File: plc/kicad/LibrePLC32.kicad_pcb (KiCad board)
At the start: 4 copper layers, 285 parts, among them CN1 DB128V-5.08-2P-GN-S, CN10 DB128V-5.08-6P-GN-S, CN11 DB2ERC-5.08-4P, CN12 DB2ERC-5.08-4P, CN2 DB128V-5.08-2P-GN-S, CN3 DB128V-5.08-2P-GN-S, CN4 DB128V-5.08-2P-GN-S, CN5 DB128V-5.08-2P-GN-S, CN6 DB128V-5.08-2P-GN-S, CN7 DB128V-5.08-2P-GN-S, CN8 DB128V-5.08-2P-GN-S, CN9 DB128V-5.08-2P-GN-S, J2 Conn_01x04_Pin, J3 Conn_01x02_Pin, Q1 AO3400A, Q2 AO3400A, Q3 L8050QLT1G, Q4 L8050QLT1G, Q5 BSS138LT1G, Q6 CSD19537Q3, SW1 TSD003B08026A03, SW2 TSD003B08026A03, SW3 TSD003B08026A03, SW4 MSK12C02, SW5 MSK12C02, U1 TCA9535PWR, U10 ESP32-S3-MINI-1U, U11 BS-0601-SK-4W, U12 AHT20_C2757850, U13 CP2102N-A02-GQFN28R, U14 LMR16006XDDCR, U15 TPS7A5201QRGRRQ1, U16 TPS26630RGER, U18 TCAN337DR, U19 THVD1450DR, U2 TPS272C45DRHFR, U20 W5500, U21 TPS54560BDDAR, U3 TPS272C45DRHFR, U4 ADS1115IDGSR, U5 LTV-814S-TA1-A, U6 LTV-814S-TA1-A, U7 LTV-814S-TA1-A, U8 LTV-814S-TA1-A, U9 RV-3028-C7, X1 X322525MRB4SI

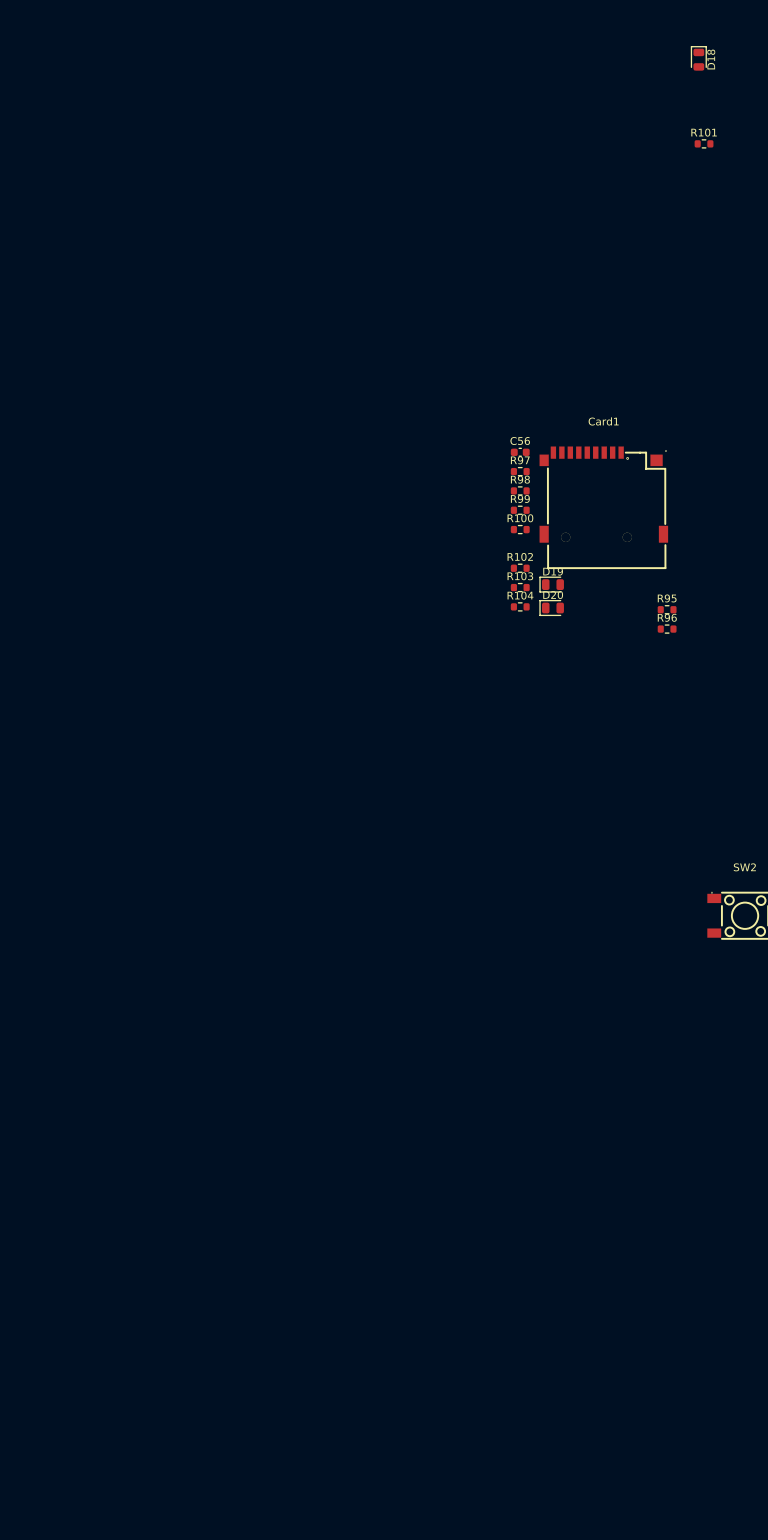
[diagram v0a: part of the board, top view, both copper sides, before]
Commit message: SD Card PCB Placement
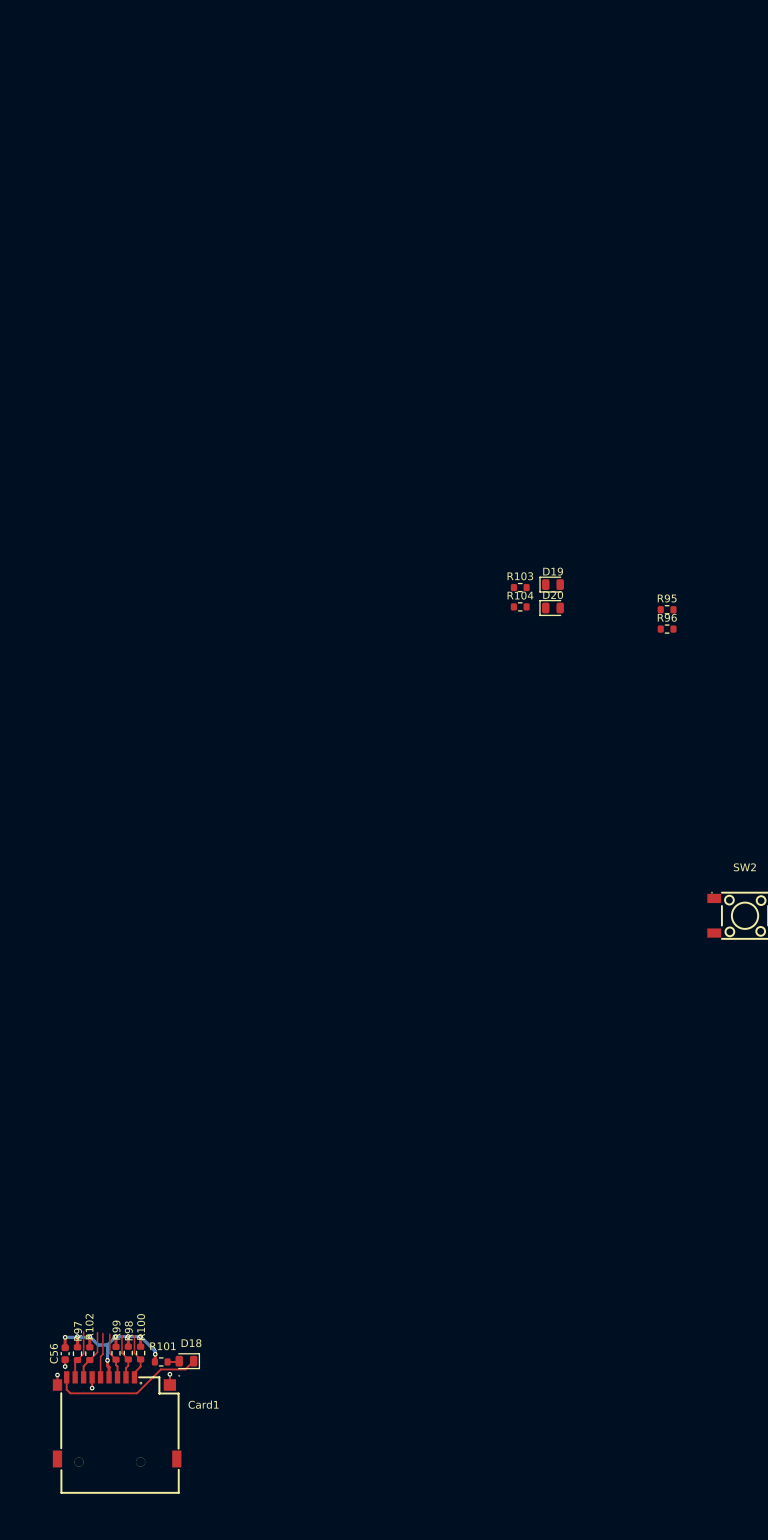
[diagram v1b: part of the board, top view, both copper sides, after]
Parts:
- moved D18 181.7 mm to (6.95, 280.1), turned to 180 degrees
- moved R101 173.2 mm to (3.67, 280.2), turned to 180 degrees
- moved Card1 135.7 mm to (-2.05, 287.5)
- moved C56 131.1 mm to (-8.80, 279.1), turned to 90 degrees
- moved R97 128.2 mm to (-7.20, 279.1), turned to 90 degrees
- moved R98 123.0 mm to (-0.60, 279.1), turned to 90 degrees
- moved R99 121.4 mm to (-2.20, 279.1), turned to 90 degrees
- moved R100 117.8 mm to (1.00, 279.1), turned to 90 degrees
- moved R102 116.3 mm to (-5.60, 279.1), turned to 90 degrees
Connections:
- Card1 pad CD: GND -> /MCU/SD_CD
- D18 pad 1: GND -> /MCU/SD_CD
- TP7 pad 1: GND -> /MCU/SD_CD
- U10 pad 11: GND -> /MCU/SD_CD
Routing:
- net +3V3: track 60.4 -> 87.5 mm, vias 5 -> 13
- net /MCU/SD_CD: track 0.00 -> 20.3 mm
- net /Ethernet/SPI_MISO: track 10.6 -> 17.1 mm
- net /MCU/SD_DAT1: track 0.00 -> 6.36 mm
- net /MCU/SD_DAT2: track 0.00 -> 6.06 mm
- net /Ethernet/SPI_MOSI: track 9.64 -> 15.7 mm
- net /MCU/~{SD_CS}: track 0.00 -> 5.88 mm
- net /Ethernet/SPI_SCLK: track 11.6 -> 17.4 mm
- net GND: track 97.2 -> 102.1 mm, vias 78 -> 82
- net Net-(D18-A): track 0.00 -> 1.55 mm

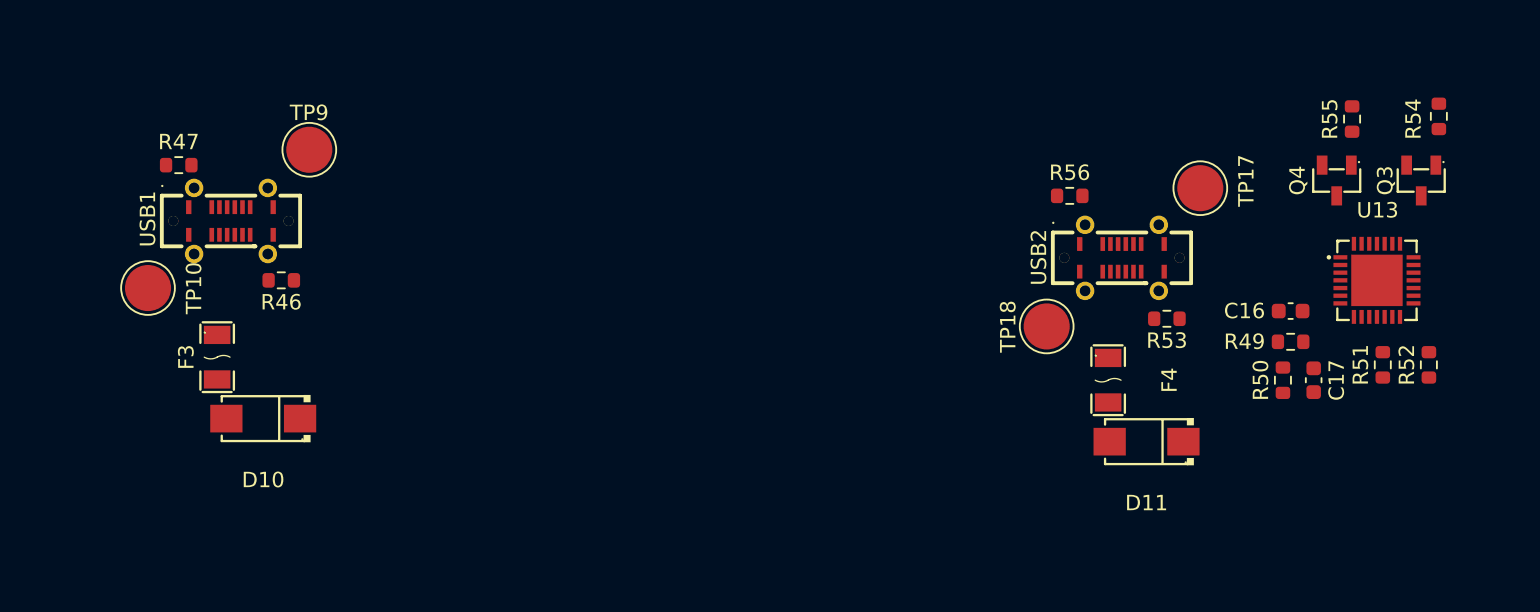
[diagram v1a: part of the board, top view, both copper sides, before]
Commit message: PCB placement of USB circuits
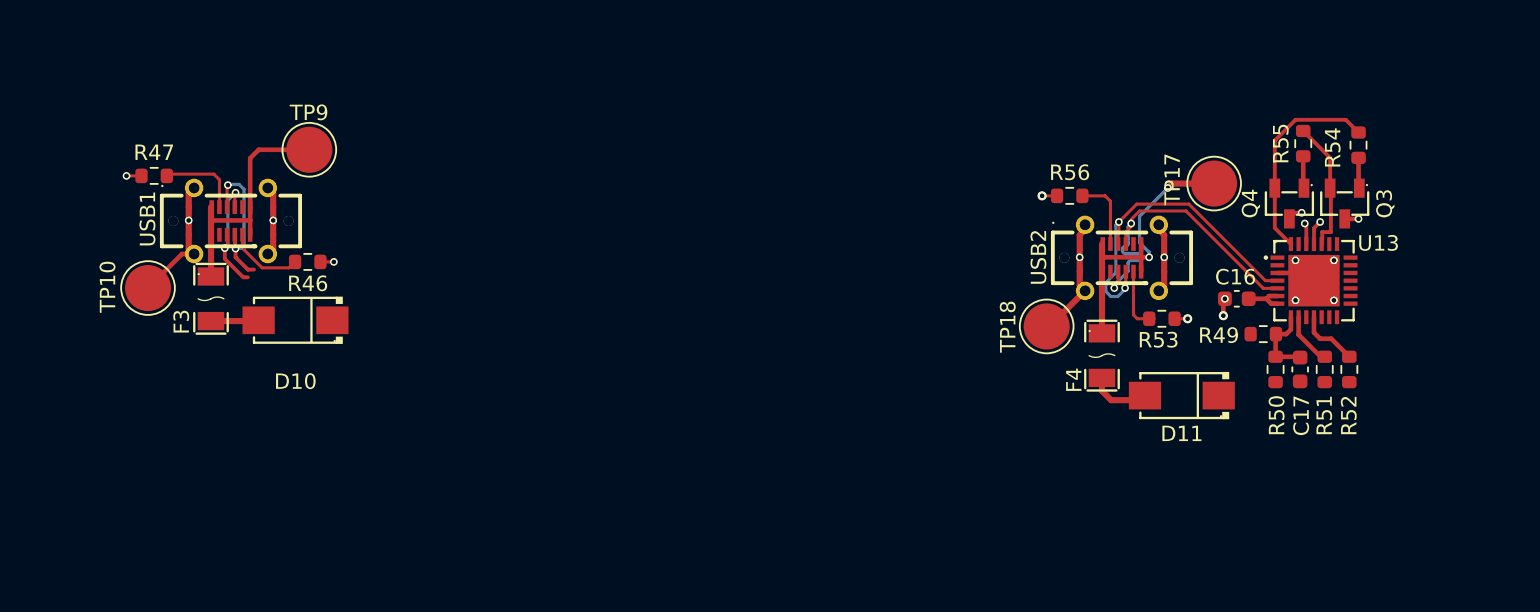
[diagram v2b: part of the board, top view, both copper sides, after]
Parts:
- C17: value 100n -> 1u
- R52: value 1k -> 10k
- moved D10 6.74 mm to (-93.4, -43.4)
- moved R54 5.56 mm to (-24.2, -54.8)
- moved Q3 5.20 mm to (-25.1, -51.0)
- moved R52 5.19 mm to (-24.8, -40.2)
- moved U13 4.10 mm to (-27.1, -46.0)
- moved F3 3.82 mm to (-98.9, -44.8)
- moved R51 3.79 mm to (-26.4, -40.2)
- moved D11 3.78 mm to (-35.7, -38.5)
- moved C16 3.60 mm to (-32.1, -44.8)
- moved R55 3.56 mm to (-27.8, -54.9)
- moved Q4 3.43 mm to (-28.7, -51.0)
- moved R46 2.10 mm to (-92.6, -47.2)
- moved R49 1.85 mm to (-30.4, -42.5)
- moved R47 1.75 mm to (-102.6, -52.8)
- moved F4 1.65 mm to (-40.9, -41.1)
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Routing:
- net GND: track 102.1 -> 135.2 mm, vias 82 -> 96
- net VDBG: track 0.00 -> 24.6 mm, vias 0 -> 2
- net /MCU/USB_D+: track 0.00 -> 21.9 mm, vias 0 -> 2
- net /MCU/USB_D-: track 0.00 -> 21.3 mm, vias 0 -> 2
- net VBUS: track 0.00 -> 16.2 mm
- net /MCU/UART_DTR: track 0.00 -> 13.5 mm
- net /MCU/MCU_USB_D+: track 0.00 -> 9.98 mm, vias 0 -> 2
- net /MCU/UART_RTS: track 0.00 -> 8.69 mm
- net /MCU/MCU_USB_D-: track 0.00 -> 8.51 mm, vias 0 -> 2
- net Net-(USB1-CC1): track 0.00 -> 5.41 mm
- net Net-(U13-VBUS): track 0.00 -> 5.00 mm
- net Net-(USB1-CC2): track 0.00 -> 4.99 mm
- net Net-(USB2-CC1): track 0.00 -> 4.75 mm
- net Net-(USB2-CC2): track 0.00 -> 4.27 mm
- net Net-(D11-A): track 0.00 -> 4.02 mm
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
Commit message: Rearranged small PCB placements
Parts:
- moved D15 278.3 mm to (436.8, 169.0)
- moved F5 275.5 mm to (441.1, 166.0), turned to 180 degrees
- moved D16 273.6 mm to (435.2, 94.6)
- moved F6 271.3 mm to (439.6, 91.4), turned to 180 degrees
- moved U1 148.1 mm to (-156.0, 263.1)
- moved R23 135.6 mm to (-160.9, 268.2)
- moved F1 52.1 mm to (-94.3, 97.7), turned to -90 degrees
- moved C15 25.6 mm to (261.3, 111.9)
- moved D12 22.2 mm to (-71.5, -39.4)
- moved F3 22.2 mm to (-77.0, -40.8)
- moved R46 22.2 mm to (-70.7, -43.1)
- moved R47 22.2 mm to (-80.7, -48.8)
- moved TP10 22.2 mm to (-81.1, -41.5)
- moved TP9 22.2 mm to (-70.6, -50.5)
- moved USB1 22.2 mm to (-75.7, -45.8)
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- renumbered C56 to C18, C18 to C20, C20 to C21, C21 to C22, C22 to C23, C23 to C24, C24 to C25, C25 to C26, C26 to C27, C27 to C28, C28 to C29, C29 to C30, C30 to C31, C31 to C32, C32 to C33, C33 to C34, C34 to C35, C35 to C36, C36 to C37, C57 to C38, C38 to C39, C39 to C40, C37 to C41, C40 to C42, C41 to C43, C42 to C44, C43 to C45, C44 to C46, C45 to C47, C46 to C48, C47 to C49, C48 to C50, C59 to C51, C49 to C52, C50 to C53, C51 to C54, C58 to C55, C52 to C56, C53 to C57, C55 to C58, C54 to C59, D2 to D1, D8 to D10, D9 to D11, D10 to D12, D11 to D13, D12 to D15, D13 to D16, D15 to D17, D16 to D18, D17 to D19, D3 to D2, D20 to D3, D19 to D4, D18 to D5, D4 to D6, D5 to D7, D6 to D8, D7 to D9, L2 to L1, L4 to L2, R87 to R100, R88 to R101, R89 to R102, R90 to R103, R112 to R104, R111 to R105, R109 to R106, R110 to R107, R113 to R108, R116 to R109, R114 to R110, R115 to R111, R91 to R112, R92 to R113, R93 to R114, R103 to R49, R104 to R50, R102 to R51, R101 to R52, R99 to R53, R98 to R54, R49 to R55, R97 to R56, R50 to R57, R100 to R58, R51 to R59, R52 to R60, R53 to R61, R54 to R62, R55 to R63, R56 to R64, R57 to R65, R58 to R66, R59 to R67, R60 to R68, R61 to R69, R62 to R70, R63 to R71, R64 to R72, R65 to R73, R67 to R74, R105 to R75, R69 to R76, R70 to R77, R71 to R78, R72 to R79, R73 to R80, R74 to R81, R75 to R82, R76 to R83, R77 to R84, R78 to R85, R106 to R86, R107 to R87, R108 to R88, R79 to R89, R80 to R90, R95 to R91, R96 to R92, R94 to R93, R81 to R94, R82 to R95, R83 to R96, R84 to R97, R85 to R98, R86 to R99, TP28 to TP24, TP24 to TP25, TP25 to TP26, TP26 to TP27, TP27 to TP28, U21 to U15, U15 to U17
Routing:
- net GND: track 135.2 -> 204.5 mm, vias 96 -> 138
- net Vbat: track 0.00 -> 19.2 mm
- net Net-(CN1-Pad1): track 0.00 -> 18.6 mm
- net +3V3: track 90.4 -> 105.7 mm
- net Net-(U18-RXD): track 0.00 -> 6.73 mm
- net Net-(U18-TXD): track 0.00 -> 6.66 mm
- net /MCU/I2C_SCL: track 0.00 -> 4.35 mm
- net PWR_CAN: track 0.00 -> 3.72 mm
- net PWR_RS485: track 0.00 -> 3.62 mm
- net Net-(D16-A): track 0.00 -> 3.41 mm
- net Net-(D15-A): track 0.00 -> 3.21 mm
- net /Terminal Blocks Interface/~{GPIO_MUX_INT}: track 0.00 -> 2.30 mm
- net V_FIELD: track 0.00 -> 2.20 mm
- net /MCU/I2C_SDA: track 0.00 -> 2.20 mm
- net /MCU/~{RTC_INT}: track 0.00 -> 1.82 mm
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
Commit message: TPS272C45 PCB placement
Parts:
- moved R92 354.7 mm to (424.1, 180.8), turned to 180 degrees
- moved R91 354.7 mm to (424.0, 176.2), turned to 180 degrees
- moved U4 121.3 mm to (-160.2, 192.8), turned to -90 degrees
- moved R14 116.3 mm to (-169.7, 210.1), turned to 180 degrees
- moved U3 113.6 mm to (-164.3, 212.2)
- moved R15 111.0 mm to (-166.8, 207.6), turned to -90 degrees
- moved R20 108.5 mm to (-169.7, 211.7), turned to 180 degrees
- moved R2 107.3 mm to (-161.8, 207.7), turned to 90 degrees
- moved C6 106.4 mm to (-169.7, 214.2), turned to 180 degrees
- moved C4 106.0 mm to (-169.7, 208.5), turned to 180 degrees
- moved R4 104.1 mm to (-164.4, 204.6), turned to 90 degrees
- moved R6 103.5 mm to (-165.2, 207.6), turned to 90 degrees
- moved U2 103.2 mm to (-148.2, 212.2)
- moved R16 102.3 mm to (-158.3, 206.9)
- moved R17 100.0 mm to (-153.4, 211.7), turned to 180 degrees
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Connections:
- CN10 pad 3: /Terminal Blocks Interface/T1_OUT1 -> /Terminal Blocks Interface/T1_OUT2
- CN10 pad 4: /Terminal Blocks Interface/T1_OUT2 -> /Terminal Blocks Interface/T1_OUT1
- CN10 pad 5: /Terminal Blocks Interface/T2_OUT1 -> /Terminal Blocks Interface/T2_OUT2
- CN10 pad 6: /Terminal Blocks Interface/T2_OUT2 -> /Terminal Blocks Interface/T2_OUT1
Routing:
- net /Terminal Blocks Interface/T1_OUT1: track 0.00 -> 24.8 mm, vias 0 -> 6
- net /Terminal Blocks Interface/T2_OUT2: track 0.00 -> 24.1 mm, vias 0 -> 6
- net /Terminal Blocks Interface/T1_OUT2: track 0.00 -> 21.7 mm, vias 0 -> 6
- net /Terminal Blocks Interface/T2_OUT1: track 0.00 -> 21.6 mm, vias 0 -> 6
- net GND: track 204.5 -> 222.6 mm, vias 138 -> 150
- net +3V3: track 105.7 -> 120.6 mm, vias 13 -> 21
- net /Terminal Blocks Interface/T1_DIA: track 0.00 -> 6.85 mm
- net /Terminal Blocks Interface/T2_DIA: track 0.00 -> 6.48 mm
- net /Terminal Blocks Interface/T1_SNS: track 0.00 -> 5.76 mm
- net /Terminal Blocks Interface/T2_EN2: track 0.00 -> 5.15 mm
- net /Terminal Blocks Interface/T2_SNS: track 0.00 -> 5.11 mm
- net /Terminal Blocks Interface/T1_EN2: track 0.00 -> 5.00 mm
- net /Terminal Blocks Interface/T1_FLT1: track 0.00 -> 3.49 mm
- net /Terminal Blocks Interface/T1_SEL: track 0.00 -> 3.00 mm
- net /Terminal Blocks Interface/T2_FLT1: track 0.00 -> 2.97 mm
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- added copper zone on F.Cu, net /Terminal Blocks Interface/T1_OUT1
- added copper zone on F.Cu, net /Terminal Blocks Interface/T1_OUT2
- added copper zone on F.Cu, net /Terminal Blocks Interface/T2_OUT1
- added copper zone on F.Cu, net /Terminal Blocks Interface/T2_OUT2

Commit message: PCB placement updates
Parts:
- U10: footprint RF_Module:ESP32-S2-MINI-1U -> LibrePLC32:BULETM-SMD_ESPRESSIF_ESP32-S3-MINI-1U-N8
- moved C28 349.8 mm to (-181.9, 173.3)
- moved R71 349.8 mm to (-186.1, 170.3)
- moved R72 349.8 mm to (-186.1, 173.3)
- moved R73 349.8 mm to (-184.5, 173.3)
- moved R75 349.8 mm to (-180.3, 173.3)
- moved R77 349.8 mm to (-178.7, 173.3)
- moved R85 349.8 mm to (-173.3, 169.2)
- moved C20 349.8 mm to (-166.5, 160.0)
- moved C22 349.8 mm to (-177.9, 160.0)
- moved C23 349.8 mm to (-187.0, 160.7)
- moved C26 349.8 mm to (-159.8, 160.6)
- moved C37 349.8 mm to (-165.7, 175.9)
- moved D6 349.8 mm to (-191.6, 160.7)
- moved Q5 349.8 mm to (-189.9, 169.5)
- moved Q6 349.8 mm to (-186.7, 167.0)
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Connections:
- CN3 pad 1: Net-(CN3-Pad1) -> /Terminal Blocks Interface/RLY1_NC
- CN4 pad 1: Net-(CN4-Pad1) -> /Terminal Blocks Interface/RLY1_NO
- CN4 pad 2: Net-(CN4-Pad2) -> /Terminal Blocks Interface/RLY2_NC
- CN5 pad 2: Net-(CN5-Pad2) -> /Terminal Blocks Interface/RLY2_NO
- RLY1 pad 2: Net-(CN3-Pad1) -> /Terminal Blocks Interface/RLY1_NO
- RLY1 pad 3: Net-(CN4-Pad1) -> /Terminal Blocks Interface/RLY1_NC
- RLY2 pad 2: Net-(CN4-Pad2) -> /Terminal Blocks Interface/RLY2_NO
- RLY2 pad 3: Net-(CN5-Pad2) -> /Terminal Blocks Interface/RLY2_NC
- U10 pad 45: /MCU/~{MCU_RST} -> (no net)
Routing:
- net /Terminal Blocks Interface/DI_COM: track 0.00 -> 44.7 mm
- net +3V3: track 120.6 -> 160.7 mm, vias 21 -> 27
- net /Terminal Blocks Interface/T1_FLT1: track 3.49 -> 41.1 mm, vias 0 -> 2
- net GND: track 222.6 -> 249.9 mm, vias 150 -> 207
- net Net-(CN5-Pad1): track 0.00 -> 25.0 mm
- net Net-(CN3-Pad2): track 0.00 -> 25.0 mm
- net /Terminal Blocks Interface/T1_EN1: track 2.16 -> 26.6 mm, vias 0 -> 2
- net /Terminal Blocks Interface/T1_SEL: track 3.00 -> 26.4 mm, vias 0 -> 2
- net /Terminal Blocks Interface/T1_LATCH: track 2.42 -> 24.1 mm, vias 0 -> 2
- net /Terminal Blocks Interface/T1_ADC: track 1.54 -> 23.2 mm
- net /Terminal Blocks Interface/T1_EN2: track 5.00 -> 26.5 mm, vias 0 -> 2
- net /MCU/I2C_SDA: track 2.20 -> 22.6 mm, vias 0 -> 2
- net /Terminal Blocks Interface/T2_LATCH: track 1.85 -> 22.1 mm
- net /MCU/I2C_SCL: track 4.35 -> 24.6 mm, vias 0 -> 2
- net /Terminal Blocks Interface/T1_FLT2: track 2.41 -> 22.4 mm, vias 0 -> 2
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- added copper zone on B.Cu, net V_FIELD

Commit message: Updated PCB placement
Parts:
- removed TP1, TP2, TP3, TP4, TP5, TP6, TP7, TP8: TestPoint, TestPoint:TestPoint_Pad_D2.0mm
- added CN13: DB128V-5.08-2P-GN-S, LibrePLC32:CONN-TH_2P-P5.08_DIBO_DB128V-5.08, F.Cu at (-133.7, 243.0)
- added CN14: DB128V-5.08-2P-GN-S, LibrePLC32:CONN-TH_2P-P5.08_DIBO_DB128V-5.08, F.Cu at (-143.9, 243.0)
- CN10: value DB128V-5.08-6P-GN-S -> DB128V-5.08-2P-GN-S; footprint LibrePLC32:CONN-TH_6P-P5.08_DIBO_DB128V-5.08 -> LibrePLC32:CONN-TH_2P-P5.08_DIBO_DB128V-5.08
- moved D9 486.4 mm to (-127.5, 192.0)
- moved R76 486.4 mm to (-131.1, 192.0)
- moved C19 483.3 mm to (-138.0, 199.8)
- moved C29 483.3 mm to (-132.0, 194.4)
- moved C32 483.3 mm to (-137.2, 203.1)
- moved D7 483.3 mm to (-134.1, 203.7)
- moved D8 483.3 mm to (-130.2, 203.8)
- moved L1 483.3 mm to (-129.8, 197.2)
- moved R67 483.3 mm to (-137.3, 195.6)
- moved R68 483.3 mm to (-137.3, 193.9)
- moved TP19 483.3 mm to (-125.5, 197.2)
- moved TP20 483.3 mm to (-125.8, 205.8)
- moved U14 483.3 mm to (-134.1, 197.4)
- moved C45 413.2 mm to (-222.6, 207.7)
- moved C46 413.2 mm to (-216.1, 207.7)
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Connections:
- net Net-(D8-K) renamed /Power/AUX_SW
- CN3 pad 1: /Terminal Blocks Interface/RLY1_NC -> Net-(CN3-Pad1)
- CN3 pad 2: Net-(CN3-Pad2) -> /Terminal Blocks Interface/RLY1_NC
- CN4 pad 1: /Terminal Blocks Interface/RLY1_NO -> /Terminal Blocks Interface/RLY2_NC
- CN4 pad 2: /Terminal Blocks Interface/RLY2_NC -> /Terminal Blocks Interface/RLY1_NO
- CN5 pad 1: Net-(CN5-Pad1) -> /Terminal Blocks Interface/RLY2_NO
- CN5 pad 2: /Terminal Blocks Interface/RLY2_NO -> Net-(CN5-Pad2)
- RLY1 pad 5: Net-(CN3-Pad2) -> Net-(CN3-Pad1)
- RLY2 pad 5: Net-(CN5-Pad1) -> Net-(CN5-Pad2)
- U10 pad 10: /MCU/SD_CS -> /Ethernet/SPI_MOSI
- U10 pad 11: /MCU/SD_CD -> /MCU/~{SD_CS}
- U10 pad 12: Net-(U10-IO8) -> /Ethernet/~{ETH_CS}
- U10 pad 13: /MCU/ADC_RDY -> /MCU/SD_CD
- U10 pad 15: /Ethernet/SPI_MOSI -> unconnected-(U10-IO11-Pad15)
- U10 pad 16: /Ethernet/SPI_SCLK -> /MCU/ADC_RDY
- U10 pad 17: /Ethernet/SPI_MISO -> unconnected-(U10-IO13-Pad17)
- U10 pad 18: /Ethernet/~{ETH_CS} -> unconnected-(U10-IO14-Pad18)
- U10 pad 45: (no net) -> unconnected-(U10-EN-Pad45)
- U10 pad 5: Net-(U10-IO1) -> /MCU/~{RTC_INT}
- U10 pad 8: /MCU/~{RTC_INT} -> /Ethernet/SPI_MISO
- U10 pad 9: Net-(U10-IO5) -> /Ethernet/SPI_SCLK
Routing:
- net /Power/V_IN_MAIN: track 12.2 -> 58.0 mm, vias 0 -> 4
- net /Terminal Blocks Interface/MOS_IN1: track 0.00 -> 40.6 mm
- net /Ethernet/~{ETH_INT}: track 3.88 -> 39.7 mm, vias 0 -> 2
- net /Ethernet/~{ETH_RST}: track 8.55 -> 40.4 mm, vias 0 -> 2
- net +3V3_AUX: track 14.7 -> 44.3 mm, vias 0 -> 2
- net GND: track 249.9 -> 279.3 mm, vias 207 -> 296
- net /Ethernet/SPI_MOSI: track 15.7 -> 44.0 mm, vias 0 -> 2
- net Net-(CN5-Pad2): track 0.00 -> 25.0 mm
- net Net-(CN5-Pad1): track 25.0 -> 0.00 mm
- net Net-(CN3-Pad1): track 0.00 -> 25.0 mm
- net Net-(CN3-Pad2): track 25.0 -> 0.00 mm
- net /MCU/~{MCU_BOOT}: track 0.97 -> 25.7 mm, vias 1 -> 2
- net /Terminal Blocks Interface/MOS_IN2: track 0.00 -> 24.8 mm
- net /Ethernet/~{ETH_CS}: track 12.9 -> 35.6 mm, vias 0 -> 4
- net /Ethernet/SPI_SCLK: track 17.4 -> 39.0 mm
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- added copper zone on F.Cu, net /Power/AUX_SW
- added copper zone on B.Cu, net GND
- removed copper zone on F.Cu, net +3V3_AUX
